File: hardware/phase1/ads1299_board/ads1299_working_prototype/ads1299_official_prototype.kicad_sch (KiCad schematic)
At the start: 139 parts, among them J2 1725656, J3 TSM-110-01-T-DV-P-TR, J6 36PIN_IDC, J80 Conn_02x16_Odd_Even, J81 Conn_02x16_Odd_Even, J9 1725656, U1 ADS1299IPAG, U10 24AA256-I/ST, U11 OPA376AID, U4 OPA376, U5 TPS60403DBVT, U6 TPS73225DBVT, U7 TPS72325DBVT

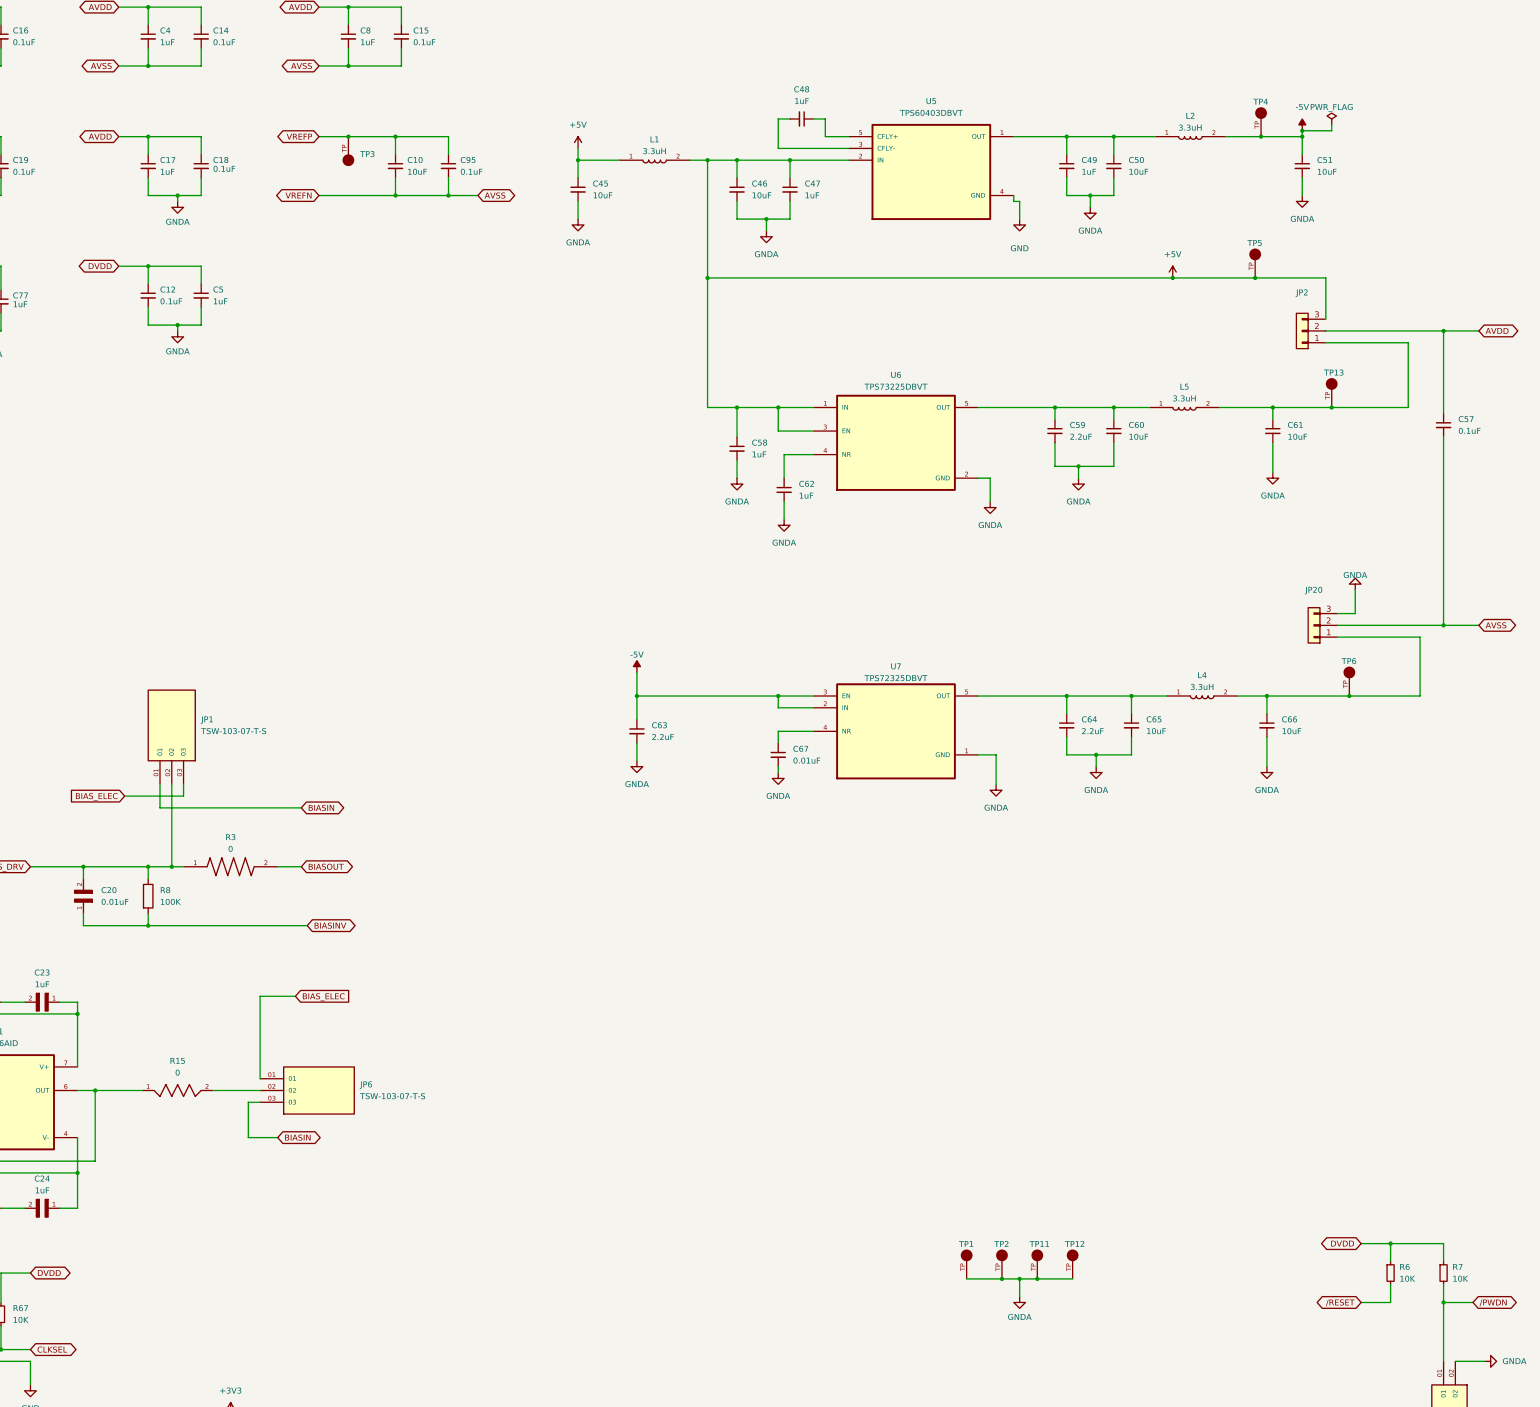
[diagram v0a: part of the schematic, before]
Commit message: Only thing left is the AVDD power routing, not sure if we can just connect that to power plane or not. Also ground plane, then done
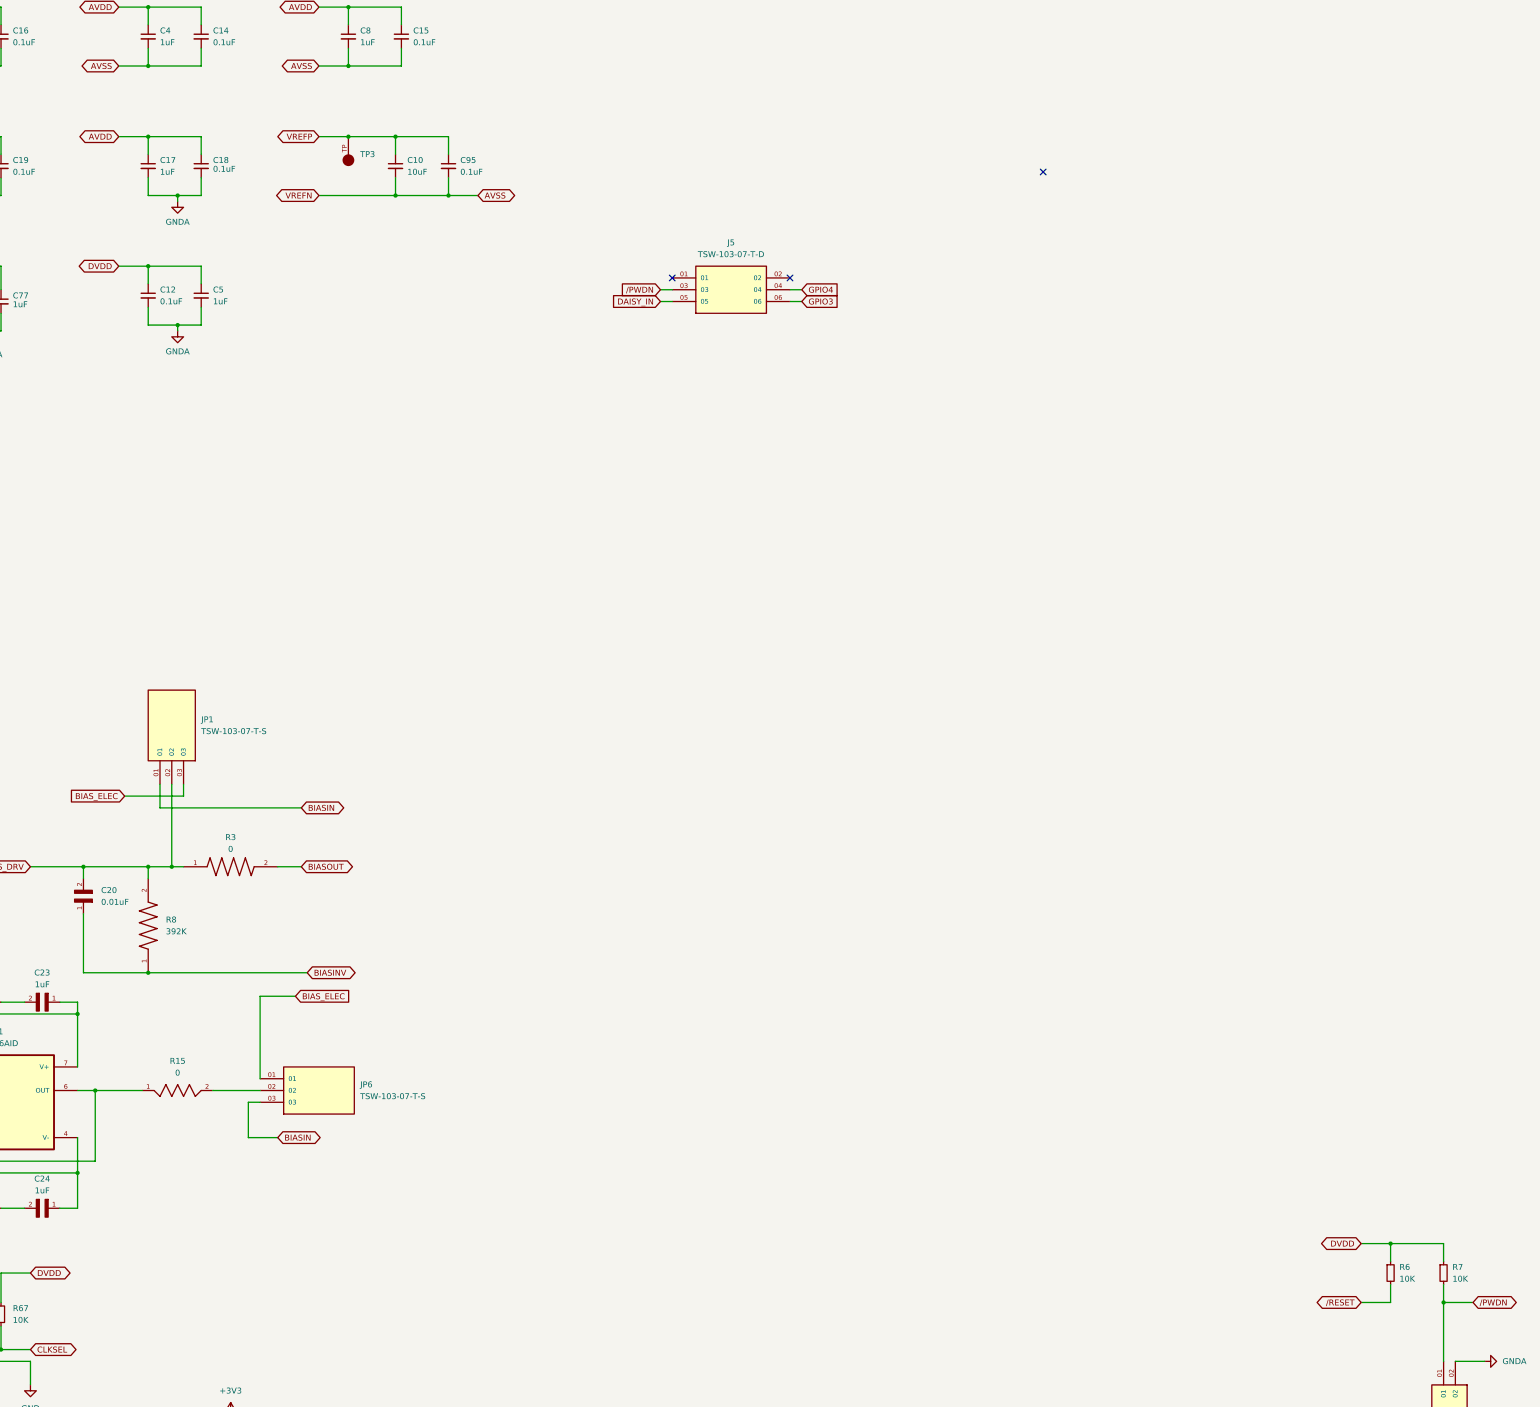
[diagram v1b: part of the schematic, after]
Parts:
- removed C45, C46, C50, C51, C60, C61, C65, C66: 10uF, symbol Device:C_Small
- removed C47, C48, C49, C58, C62: 1uF, symbol Device:C_Small
- removed C57: 0.1uF, symbol Device:C_Small
- removed C59, C63, C64: 2.2uF, symbol Device:C_Small
- removed C67: 0.01uF, symbol Device:C_Small
- removed JP2, JP20: Conn_01x03, symbol Connector_Generic:Conn_01x03
- removed L1, L2, L4, L5: 3.3uH, MLZ2012A3R3W:INDC2012X87N, symbol MLZ2012A3R3W:MLZ2012A3R3W
- removed R8: 100K, symbol Device:R
- removed TP1, TP11, TP12, TP13, TP2, TP4, TP5, TP6: 5001, 5001:KEYSTONE_5001, symbol 5001:5001
- removed U5: TPS60403DBVT, TPS60403DBVT:SOT95P280X145-5N, symbol TPS60403DBVT:TPS60403DBVT
- removed U6: TPS73225DBVT, TPS73225DBVT:SOT95P280X145-5N, symbol TPS73225DBVT:TPS73225DBVT
- removed U7: TPS72325DBVT, TPS72325DBVT:SOT95P280X145-5N, symbol TPS72325DBVT:TPS72325DBVT
- added J5: TSW-103-07-T-D, TSW-103-07-T-D:SAMTEC_TSW-103-07-T-D, symbol TSW-103-07-T-D:TSW-103-07-T-D
- added R8: 392K, RC0603FR-07392KL:RESC1608X55N, symbol RC0603FR-07392KL:RC0603FR-07392KL
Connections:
- net BIASINV: now also R8.1
- net BIAS_DRV: now also R8.2
- net DAISY_IN: now also J5.05
- net GPIO3: now also J5.06
- net GPIO4: now also J5.04
- net /PWDN: now also J5.03
- no-connect marks 30 -> 33
